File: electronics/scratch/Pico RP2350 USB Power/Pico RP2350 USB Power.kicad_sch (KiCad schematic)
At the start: 30 parts, among them J1 RFM69HCW, J10 IR TX AOE, J11 IR RX 1, J12 IR RX 2, J13 IR RX 3, J14 BUTTON A, J15 BUTTON B, J2 SD CARD, J3 I2C_1, J4 I2C_2, J5 I2C_3, J6 I2C_STEMMA, J7 I2S AMP, J8 IR TX LINE, J9 IR TX CONE, Q1 AO3406, Q2 AO3406, Q3 AO3406, SW1 SW POWER

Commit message: USB powered main board first draft. No routing yet.
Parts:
- added J16: LED STRIP 1, Connector_PinHeader_2.54mm:PinHeader_1x03_P2.54mm_Vertical, symbol Connector:Conn_01x03_Pin
- added J17: LED STRIP 2, Connector_PinHeader_2.54mm:PinHeader_1x03_P2.54mm_Vertical, symbol Connector:Conn_01x03_Pin
- added J18: LED STRIP 3, Connector_PinHeader_2.54mm:PinHeader_1x03_P2.54mm_Vertical, symbol Connector:Conn_01x03_Pin
- added J19: LED STRIP 4, Connector_PinHeader_2.54mm:PinHeader_1x03_P2.54mm_Vertical, symbol Connector:Conn_01x03_Pin
- added J20: LED STRIP 5, Connector_PinHeader_2.54mm:PinHeader_1x03_P2.54mm_Vertical, symbol Connector:Conn_01x03_Pin
- added J21: LED STRIP 6, Connector_PinHeader_2.54mm:PinHeader_1x03_P2.54mm_Vertical, symbol Connector:Conn_01x03_Pin
- added J22: POWER, Connector_PinHeader_2.54mm:PinHeader_1x02_P2.54mm_Vertical, symbol Connector:Conn_01x02_Pin
- added Q4: AO3401A, Package_TO_SOT_SMD:SOT-23, symbol Transistor_FET:AO3401A
- added Q5: C20917, Package_TO_SOT_SMD:SOT-23, symbol Transistor_FET:AO3400A
- added R12, R13, R14, R15, R7, R8: 100, Resistor_SMD:R_0805_2012Metric, symbol Device:R
- added R16, R17: 100K, Resistor_SMD:R_0805_2012Metric, symbol Device:R
- added U1: 74HCT244, Package_SO:TSSOP-20_4.4x6.5mm_P0.65mm, symbol 74xx:74HCT244
- A1: footprint Module:RaspberryPi_Pico_Common_Unspecified -> Module:RaspberryPi_Pico_Common_THT
- SW1: value SW POWER -> POWER; footprint Button_Switch_THT:SW_DIP_SPSTx01_Slide_9.78x4.72mm_W7.62mm_P2.54mm -> (none)
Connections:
- net +3.3V: now also D2.2 (A)
- net 3V3_EN: now also SW1.1 (A), J22.2 (Pin_2)
- net BUTTON A: now also A1.31 (GPIO26_ADC0); no longer A1.32 (GPIO27_ADC1)
- net BUTTON B: now also A1.32 (GPIO27_ADC1); no longer A1.34 (GPIO28_ADC2)
- net GND: now also SW1.2 (B), J16.1 (Pin_1), J17.1 (Pin_1), J18.1 (Pin_1), J19.1 (Pin_1), J20.1 (Pin_1), J21.1 (Pin_1), J22.1 (Pin_1), Q5.2 (S), R17.1, U1.1 (1OE), U1.10 (GND), U1.11 (2A3), U1.13 (2A2), U1.19 (2OE)
- net LED STRIP 1: now also U1.17 (2A0)
- net LED STRIP 2: now also U1.15 (2A1)
- net LED STRIP 3: now also U1.2 (1A0)
- net LED STRIP 4: now also U1.4 (1A1)
- net LED STRIP 5: now also U1.6 (1A2)
- net LED STRIP 6: now also U1.8 (1A3)
- net VBUS: now also Q4.2 (S), R16.2; no longer D2.2 (A)
- new net: J19.2 (Pin_2), R13.2
- new net: J16.2 (Pin_2), R7.2
- new net: J17.2 (Pin_2), R8.2
- new net: J21.2 (Pin_2), R15.2
- new net: J18.2 (Pin_2), R12.2
- new net: J20.2 (Pin_2), R14.2
- new net: Q4.1 (G), Q5.3 (D), R16.1
- new net +5V: J16.3 (Pin_3), J17.3 (Pin_3), J18.3 (Pin_3), J19.3 (Pin_3), J20.3 (Pin_3), J21.3 (Pin_3), Q4.3 (D), U1.20 (VCC)
- new net 5V_ENABLE: A1.34 (GPIO28_ADC2), Q5.1 (G), R17.2
- new net LED SHIFTED 1: R7.1, U1.3 (2Y0)
- new net LED SHIFTED 2: R8.1, U1.5 (2Y1)
- new net LED SHIFTED 3: R12.1, U1.18 (1Y0)
- new net LED SHIFTED 4: R13.1, U1.16 (1Y1)
- new net LED SHIFTED 5: R14.1, U1.14 (1Y2)
- new net LED SHIFTED 6: R15.1, U1.12 (1Y3)
- no-connect marks 4 -> 5
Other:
- note added: "5V POWER ENABLE"
- note added: "LED STRIPS"
- moved on the sheet: D2, R9

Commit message: More pinout labels, removed some component labels, fixed STEMMA MP ground.
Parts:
- removed J6: I2C_STEMMA, Connector_JST:JST_SH_BM04B-SRSS-TB_1x04-1MP_P1.00mm_Vertical, symbol Connector:Conn_01x04_Pin
- added J6: STEMMA, Connector_JST:JST_SH_BM04B-SRSS-TB_1x04-1MP_P1.00mm_Vertical, symbol Connector_Generic_MountingPin:Conn_01x04_MountingPin
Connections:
- net +3.3V: now also J11.3 (Pin_3), J12.3 (Pin_3), J13.3 (Pin_3), J6.2 (Pin_2); no longer J11.1 (Pin_1), J12.1 (Pin_1), J13.1 (Pin_1)
- net GND: now also J11.1 (Pin_1), J12.1 (Pin_1), J13.1 (Pin_1), J6.1 (Pin_1), J6.MP (MountPin); no longer J11.3 (Pin_3), J12.3 (Pin_3), J13.3 (Pin_3)
- net SCL: now also J6.4 (Pin_4)
- net SDA: now also J6.3 (Pin_3)
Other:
- moved on the sheet: J11, J12, J13
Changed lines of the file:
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@@
 	(wire
 		(pts
+			(xy 167.64 100.33) (xy 163.83 100.33)
+		)
+		(stroke
+			(width 0)
+			(type default)
+		)
+	)
+	(wire
+		(pts
 			(xy 143.51 49.53) (xy 160.02 49.53)
 		)
@@
 	)
 	(symbol
-		(lib_id "Connector:Conn_01x04_Pin")
-		(at 163.83 90.17 0)
-		(mirror y)
+		(lib_id "power:GND")
+		(at 153.67 87.63 180)
 		(unit 1)
 		(body_style 1)
@@
 		(in_pos_files yes)
 		(dnp no)
-		(property "Reference" "J6"
-			(at 163.195 82.55 0)
+		(property "Reference" "#PWR010"
+			(at 153.67 81.28 0)
+			(hide yes)
 			(show_name no)
 			(do_not_autoplace no)
@@
 			)
 		)
-		(property "Value" "I2C_STEMMA"
-			(at 163.195 85.09 0)
+		(property "Value" "GND"
+			(at 153.67 83.82 0)
 			(show_name no)
 			(do_not_autoplace no)
@@
 			)
 		)
-		(property "Footprint" "Connector_JST:JST_SH_BM04B-SRSS-TB_1x04-1MP_P1.00mm_Vertical"
-			(at 163.83 90.17 0)
+		(property "Footprint" ""
+			(at 153.67 87.63 0)
 			(hide yes)
 			(show_name no)
@@
 		)
 		(property "Datasheet" ""
-			(at 163.83 90.17 0)
+			(at 153.67 87.63 0)
 			(hide yes)
 			(show_name no)
@@
 			)
 		)
-		(property "Description" "Generic connector, single row, 01x04, script generated"
-			(at 163.83 90.17 0)
+		(property "Description" "Power symbol creates a global label with name \"GND\" , ground"
+			(at 153.67 87.63 0)
 			(hide yes)
 			(show_name no)
@@
 		(pin "1"
 		)
-		(pin "2"
-		)
-		(pin "4"
-		)
-		(pin "3"
-		)
 		(instances
 			(project "Pico RP2350 USB Power"
 				(path "/f607a6cb-1f81-4ea5-ae65-67dd06ab9fb6"
-					(reference "J6")
+					(reference "#PWR010")
 					(unit 1)
 				)
@@
 	(symbol
 		(lib_id "power:GND")
-		(at 153.67 87.63 180)
+		(at 167.64 100.33 0)
 		(unit 1)
 		(body_style 1)
@@
 		(in_pos_files yes)
 		(dnp no)
-		(property "Reference" "#PWR010"
-			(at 153.67 81.28 0)
+		(property "Reference" "#PWR042"
+			(at 167.64 106.68 0)
 			(hide yes)
 			(show_name no)
@@
 		)
 		(property "Value" "GND"
-			(at 153.67 83.82 0)
+			(at 167.64 104.14 0)
 			(show_name no)
 			(do_not_autoplace no)
@@
 		)
 		(property "Footprint" ""
-			(at 153.67 87.63 0)
+			(at 167.64 100.33 0)
 			(hide yes)
 			(show_name no)
@@
 		)
 		(property "Datasheet" ""
-			(at 153.67 87.63 0)
+			(at 167.64 100.33 0)
 			(hide yes)
 			(show_name no)
@@
 		)
 		(property "Description" "Power symbol creates a global label with name \"GND\" , ground"
-			(at 153.67 87.63 0)
+			(at 167.64 100.33 0)
 			(hide yes)
 			(show_name no)
@@
 			(project "Pico RP2350 USB Power"
 				(path "/f607a6cb-1f81-4ea5-ae65-67dd06ab9fb6"
-					(reference "#PWR010")
+					(reference "#PWR042")
 					(unit 1)
 				)
@@
 	)
 	(symbol
+		(lib_id "Connector_Generic_MountingPin:Conn_01x04_MountingPin")
+		(at 163.83 90.17 0)
+		(unit 1)
+		(body_style 1)
+		(exclude_from_sim no)
+		(in_bom yes)
+		(on_board yes)
+		(in_pos_files yes)
+		(dnp no)
+		(property "Reference" "J6"
+			(at 166.37 90.5255 0)
+			(show_name no)
+			(do_not_autoplace no)
+			(effects
+				(font
+					(size 1.27 1.27)
+				)
+				(justify left)
+			)
+		)
+		(property "Value" "STEMMA"
+			(at 161.036 84.074 0)
+			(show_name no)
+			(do_not_autoplace no)
+			(effects
+				(font
+					(size 1.27 1.27)
+				)
+				(justify left)
+			)
+		)
+		(property "Footprint" "Connector_JST:JST_SH_BM04B-SRSS-TB_1x04-1MP_P1.00mm_Vertical"
+			(at 163.83 90.17 0)
+			(hide yes)
+			(show_name no)
+			(do_not_autoplace no)
+			(effects
+				(font
+					(size 1.27 1.27)
+				)
+			)
+		)
+		(property "Datasheet" ""
+			(at 163.83 90.17 0)
+			(hide yes)
+			(show_name no)
+			(do_not_autoplace no)
+			(effects
+				(font
+					(size 1.27 1.27)
+				)
+			)
+		)
+		(property "Description" "Generic connectable mounting pin connector, single row, 01x04, script generated (kicad-library-utils/schlib/autogen/connector/)"
+			(at 163.83 90.17 0)
+			(hide yes)
+			(show_name no)
+			(do_not_autoplace no)
+			(effects
+				(font
+					(size 1.27 1.27)
+				)
+			)
+		)
+		(pin "MP"
+		)
+		(pin "1"
+		)
+		(pin "4"
+		)
+		(pin "2"
+		)
+		(pin "3"
+		)
+		(instances
+			(project "Pico RP2350 USB Power"
+				(path "/f607a6cb-1f81-4ea5-ae65-67dd06ab9fb6"
+					(reference "J6")
+					(unit 1)
+				)
+			)
+		)
+	)
+	(symbol
 		(lib_id "Connector:Conn_01x03_Pin")
 		(at 119.38 147.32 0)
@@
 	(symbol
 		(lib_id "Connector:Conn_01x03_Pin")
-		(at 255.27 52.07 0)
-		(mirror y)
+		(at 255.27 52.07 180)
 		(unit 1)
 		(body_style 1)
@@
 		(in_pos_files yes)
 		(dnp no)
-		(fields_autoplaced yes)
 		(property "Reference" "J12"
-			(at 256.54 50.7999 0)
+			(at 256.54 53.3401 0)
 			(show_name no)
 			(do_not_autoplace no)
@@
 		)
 		(property "Value" "IR RX 2"
-			(at 256.54 53.3399 0)
+			(at 256.54 50.8001 0)
 			(show_name no)
 			(do_not_autoplace no)
@@
 	(symbol
 		(lib_id "Connector:Conn_01x03_Pin")
-		(at 255.27 77.47 0)
-		(mirror y)
+		(at 255.27 77.47 180)
 		(unit 1)
 		(body_style 1)
@@
 		(in_pos_files yes)
 		(dnp no)
-		(fields_autoplaced yes)
 		(property "Reference" "J13"
-			(at 256.54 76.1999 0)
+			(at 256.54 78.7401 0)
 			(show_name no)
 			(do_not_autoplace no)
@@
 		)
 		(property "Value" "IR RX 3"
-			(at 256.54 78.7399 0)
+			(at 256.54 76.2001 0)
 			(show_name no)
 			(do_not_autoplace no)
@@
 	(symbol
 		(lib_id "Connector:Conn_01x03_Pin")
-		(at 255.27 26.67 0)
-		(mirror y)
+		(at 255.27 26.67 180)
 		(unit 1)
 		(body_style 1)
@@
 		(in_pos_files yes)
 		(dnp no)
-		(fields_autoplaced yes)
 		(property "Reference" "J11"
-			(at 256.54 25.3999 0)
+			(at 256.54 27.9401 0)
 			(show_name no)
 			(do_not_autoplace no)
@@
 		)
 		(property "Value" "IR RX 1"
-			(at 256.54 27.9399 0)
+			(at 256.54 25.4001 0)
 			(show_name no)
 			(do_not_autoplace no)

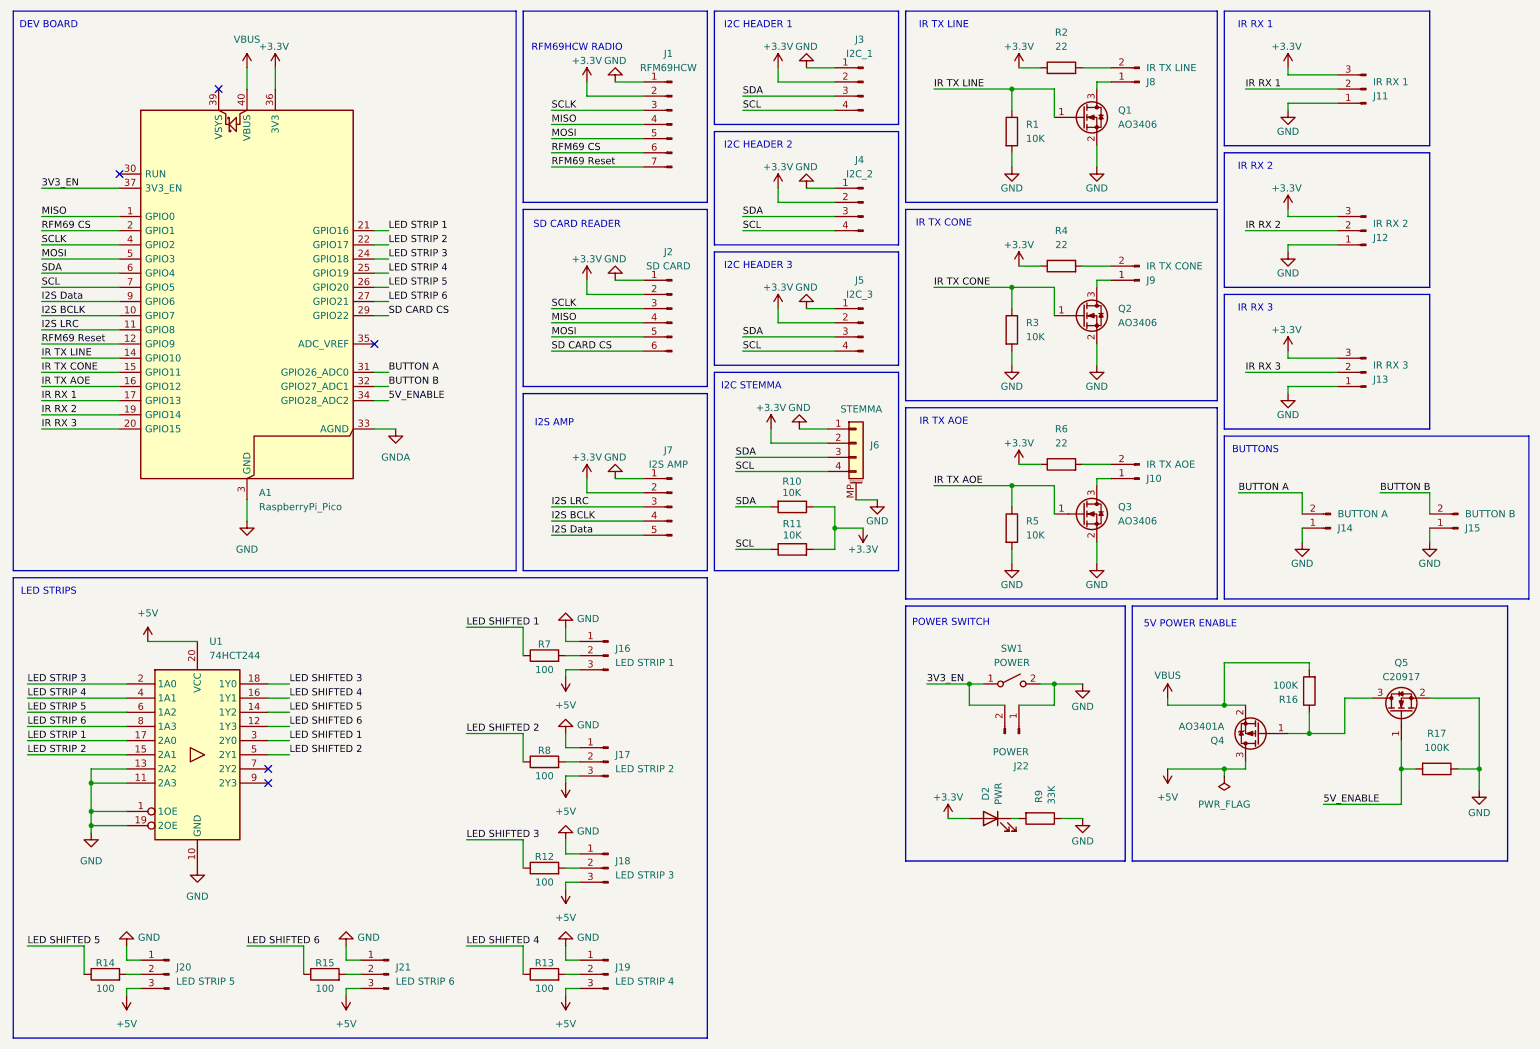
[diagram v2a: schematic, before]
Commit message: Minor cleanup of USB power main board
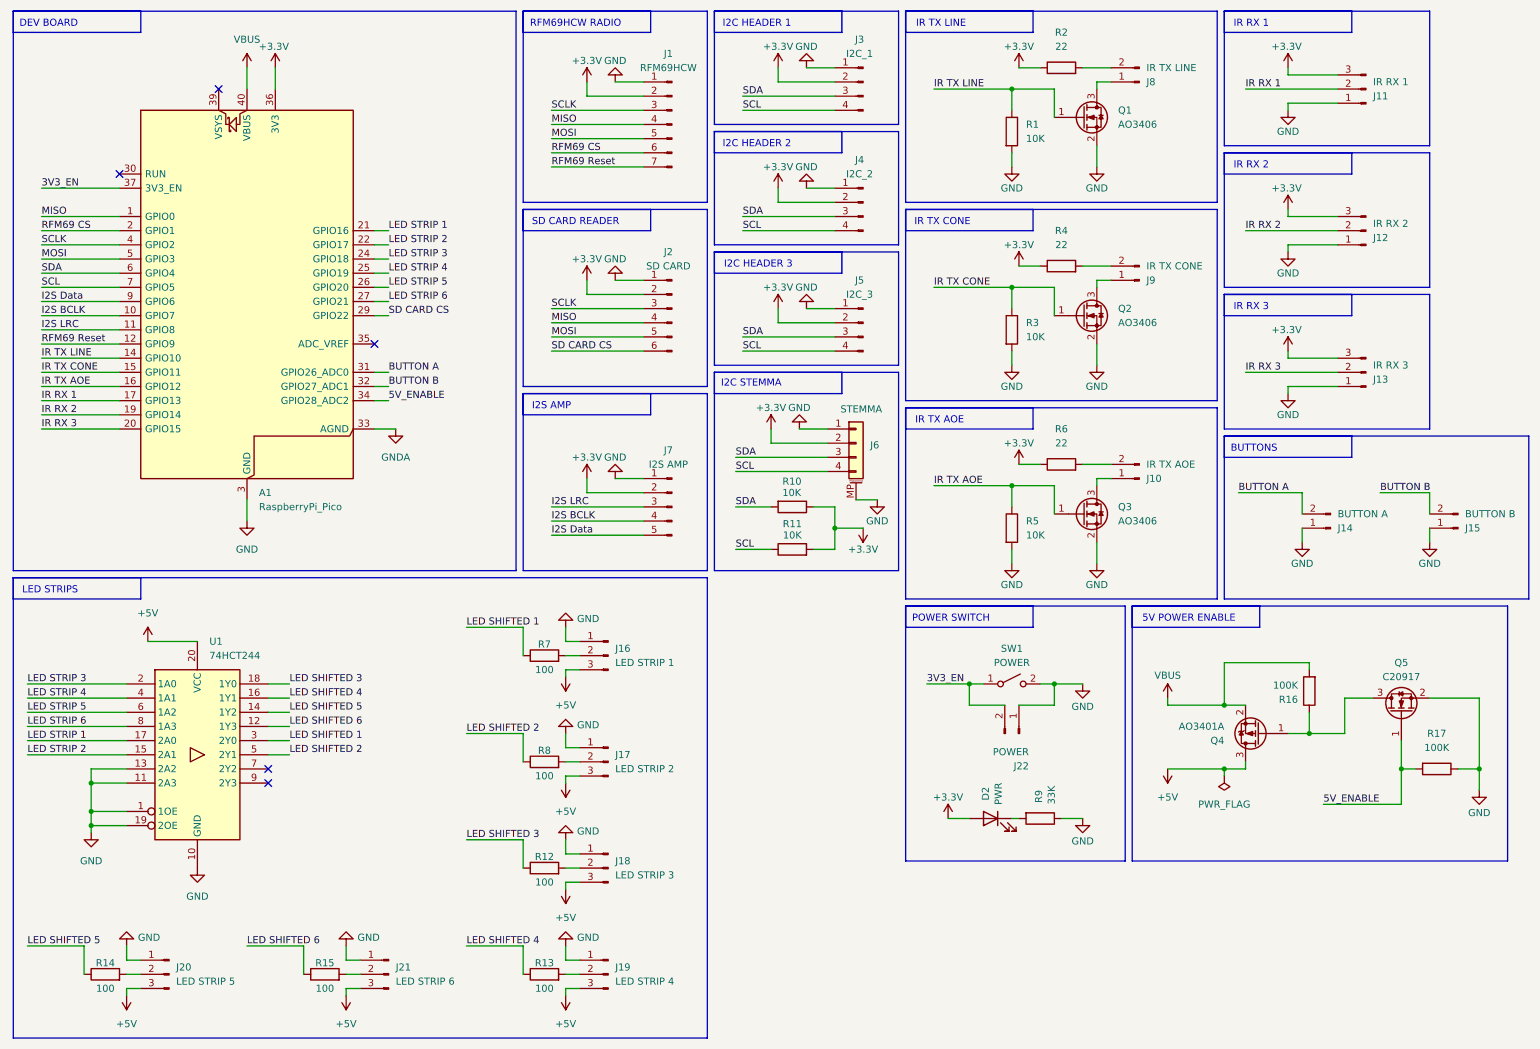
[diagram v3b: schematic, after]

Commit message: Working on 5V power fills for 3 amps
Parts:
- A1, J1, J10, J11, J12, J13, J14, J15, J16, J17, J18, J19, J2, J20, J21, J22, J3, J4, J5, J7, J8, J9: now not fitted; now left out of the parts list
- SW1: footprint (none) -> Button_Switch_THT:SW_DIP_SPSTx01_Slide_9.78x4.72mm_W7.62mm_P2.54mm; now not fitted; now left out of the parts list
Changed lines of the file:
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@@
 		(body_style 1)
 		(exclude_from_sim no)
-		(in_bom yes)
+		(in_bom no)
 		(on_board yes)
 		(in_pos_files yes)
-		(dnp no)
+		(dnp yes)
 		(fields_autoplaced yes)
 		(property "Reference" "J19"
@@
 		(body_style 1)
 		(exclude_from_sim no)
-		(in_bom yes)
+		(in_bom no)
 		(on_board yes)
 		(in_pos_files yes)
-		(dnp no)
+		(dnp yes)
 		(property "Reference" "J15"
 			(at 273.05 105.4101 0)
@@
 		(body_style 1)
 		(exclude_from_sim no)
-		(in_bom yes)
+		(in_bom no)
 		(on_board yes)
 		(in_pos_files yes)
-		(dnp no)
+		(dnp yes)
 		(property "Reference" "J5"
 			(at 164.465 60.96 0)
@@
 		(body_style 1)
 		(exclude_from_sim no)
-		(in_bom yes)
+		(in_bom no)
 		(on_board yes)
 		(in_pos_files yes)
-		(dnp no)
+		(dnp yes)
 		(property "Reference" "J2"
 			(at 130.175 55.88 0)
@@
 		(body_style 1)
 		(exclude_from_sim no)
-		(in_bom yes)
+		(in_bom no)
 		(on_board yes)
 		(in_pos_files yes)
-		(dnp no)
+		(dnp yes)
 		(fields_autoplaced yes)
 		(property "Reference" "J21"
@@
 		(body_style 1)
 		(exclude_from_sim no)
-		(in_bom yes)
+		(in_bom no)
 		(on_board yes)
 		(in_pos_files yes)
-		(dnp no)
+		(dnp yes)
 		(property "Reference" "J8"
 			(at 215.9 25.4001 0)
@@
 		(body_style 1)
 		(exclude_from_sim no)
-		(in_bom yes)
+		(in_bom no)
 		(on_board yes)
 		(in_pos_files yes)
-		(dnp no)
+		(dnp yes)
 		(fields_autoplaced yes)
 		(property "Reference" "J17"
@@
 		(body_style 1)
 		(exclude_from_sim no)
-		(in_bom yes)
+		(in_bom no)
 		(on_board yes)
 		(in_pos_files yes)
-		(dnp no)
+		(dnp yes)
 		(property "Reference" "J7"
 			(at 130.175 91.44 0)
@@
 		(body_style 1)
 		(exclude_from_sim no)
-		(in_bom yes)
+		(in_bom no)
 		(on_board yes)
 		(in_pos_files yes)
-		(dnp no)
+		(dnp yes)
 		(property "Reference" "J14"
 			(at 250.19 105.4101 0)
@@
 		(body_style 1)
 		(exclude_from_sim no)
-		(in_bom yes)
+		(in_bom no)
 		(on_board yes)
 		(in_pos_files yes)
-		(dnp no)
+		(dnp yes)
 		(fields_autoplaced yes)
 		(property "Reference" "J20"
@@
 		(body_style 1)
 		(exclude_from_sim no)
-		(in_bom yes)
+		(in_bom no)
 		(on_board yes)
 		(in_pos_files yes)
-		(dnp no)
+		(dnp yes)
 		(property "Reference" "J3"
 			(at 164.465 17.78 0)
@@
 		(body_style 1)
 		(exclude_from_sim no)
-		(in_bom yes)
+		(in_bom no)
 		(on_board yes)
 		(in_pos_files yes)
-		(dnp no)
+		(dnp yes)
 		(property "Reference" "J12"
 			(at 256.54 53.3401 0)
@@
 		(body_style 1)
 		(exclude_from_sim no)
-		(in_bom yes)
+		(in_bom no)
 		(on_board yes)
 		(in_pos_files yes)
-		(dnp no)
+		(dnp yes)
 		(property "Reference" "J10"
 			(at 215.9 96.5201 0)
@@
 		(body_style 1)
 		(exclude_from_sim no)
-		(in_bom yes)
+		(in_bom no)
 		(on_board yes)
 		(in_pos_files yes)
-		(dnp no)
+		(dnp yes)
 		(fields_autoplaced yes)
 		(property "Reference" "J16"
@@
 		(body_style 1)
 		(exclude_from_sim no)
-		(in_bom yes)
+		(in_bom no)
 		(on_board yes)
 		(in_pos_files yes)
-		(dnp no)
+		(dnp yes)
 		(property "Reference" "J13"
 			(at 256.54 78.7401 0)
@@
 		(body_style 1)
 		(exclude_from_sim no)
-		(in_bom yes)
+		(in_bom no)
 		(on_board yes)
 		(in_pos_files yes)
-		(dnp no)
+		(dnp yes)
 		(fields_autoplaced yes)
 		(property "Reference" "A1"
@@
 		(body_style 1)
 		(exclude_from_sim no)
-		(in_bom yes)
+		(in_bom no)
 		(on_board yes)
 		(in_pos_files yes)
-		(dnp no)
+		(dnp yes)
 		(property "Reference" "J1"
 			(at 130.175 20.32 0)
@@
 		(body_style 1)
 		(exclude_from_sim no)
-		(in_bom yes)
+		(in_bom no)
 		(on_board yes)
 		(in_pos_files yes)
-		(dnp no)
+		(dnp yes)
 		(property "Reference" "J22"
 			(at 194.818 148.082 90)
@@
 		(body_style 1)
 		(exclude_from_sim no)
-		(in_bom yes)
+		(in_bom no)
 		(on_board yes)
 		(in_pos_files yes)
-		(dnp no)
+		(dnp yes)
 		(property "Reference" "J4"
 			(at 164.465 39.37 0)
@@
 		(body_style 1)
 		(exclude_from_sim no)
-		(in_bom yes)
+		(in_bom no)
 		(on_board yes)
 		(in_pos_files yes)
-		(dnp no)
+		(dnp yes)
 		(property "Reference" "J11"
 			(at 256.54 27.9401 0)
@@
 		(body_style 1)
 		(exclude_from_sim no)
-		(in_bom yes)
+		(in_bom no)
 		(on_board yes)
 		(in_pos_files yes)
-		(dnp no)
+		(dnp yes)
 		(fields_autoplaced yes)
 		(property "Reference" "SW1"
@@
 			)
 		)
-		(property "Footprint" ""
+		(property "Footprint" "Button_Switch_THT:SW_DIP_SPSTx01_Slide_9.78x4.72mm_W7.62mm_P2.54mm"
 			(at 191.77 133.35 0)
 			(hide yes)
@@
 		(body_style 1)
 		(exclude_from_sim no)
-		(in_bom yes)
+		(in_bom no)
 		(on_board yes)
 		(in_pos_files yes)
-		(dnp no)
+		(dnp yes)
 		(fields_autoplaced yes)
 		(property "Reference" "J18"
@@
 		(body_style 1)
 		(exclude_from_sim no)
-		(in_bom yes)
+		(in_bom no)
 		(on_board yes)
 		(in_pos_files yes)
-		(dnp no)
+		(dnp yes)
 		(property "Reference" "J9"
 			(at 215.9 60.9601 0)
